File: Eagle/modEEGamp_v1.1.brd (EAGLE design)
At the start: 111.1 x 72.4 mm, 120 parts, among them IC2 INA217P, IC204 TLC277P, IC4 INA217P, P1 20k, P203 20k, Q1 BC547, Q2 BC557, Q202 BC557, Q204 BC557, Q206 BC547, Q208 BC547, Q3 BC547, Q4 BC557

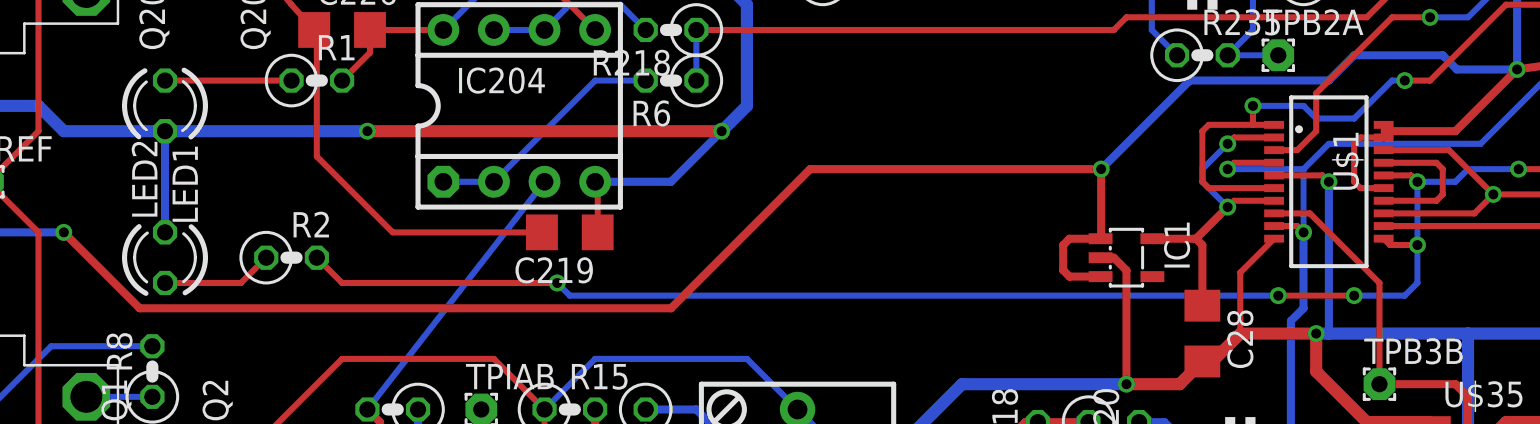
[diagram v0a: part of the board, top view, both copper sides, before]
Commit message: Updated resistor values
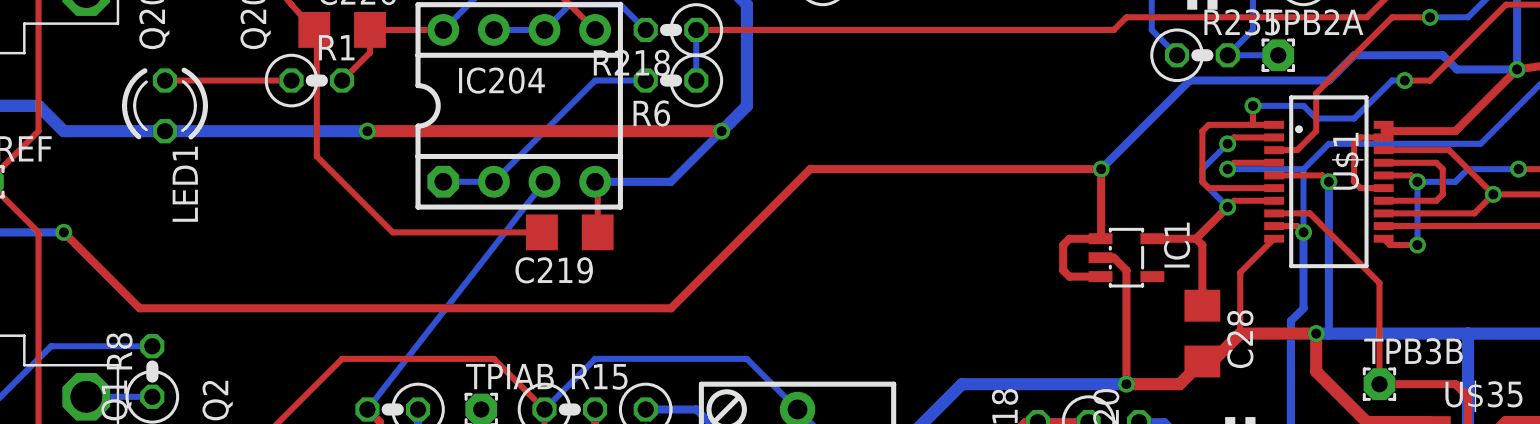
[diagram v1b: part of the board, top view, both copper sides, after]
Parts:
- removed LED2: (no value), led:LED3MM
- removed R2: (no value), resistor:0207/2V
- R1: value (none) -> 1.65k
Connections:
- removed net N$67: LED2.A, R2.1
- net AGND: no longer LED2.K
- net N$8: no longer R2.2
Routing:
- net N$8: track 87.6 -> 29.4 mm, vias 6 -> 3
- net N$67: track 5.61 -> 0.00 mm
- net AGND: track 443.4 -> 438.3 mm
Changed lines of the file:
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@@
 </element>
 <element name="LED1" library="led" package="LED3MM" value="" x="16.51" y="40.64" rot="R270"/>
-<element name="R1" library="resistor" package="0207/2V" value="" x="24.13" y="41.91"/>
-<element name="R2" library="resistor" package="0207/2V" value="" x="22.86" y="33.02"/>
-<element name="LED2" library="led" package="LED3MM" value="" x="16.51" y="33.02" rot="R90"/>
+<element name="R1" library="resistor" package="0207/2V" value="1.65k" x="24.13" y="41.91"/>
 </elements>
 <signals>
@@
 <wire x1="5.715" y1="40.64" x2="5.715" y2="41.91" width="0.4064" layer="1"/>
 <contactref element="LED1" pad="K"/>
-<contactref element="LED2" pad="K"/>
-<wire x1="16.51" y1="39.37" x2="16.51" y2="34.29" width="0.4064" layer="16"/>
 <wire x1="70.485" y1="29.21" x2="70.485" y2="32.277" width="0.3048" layer="1"/>
 <wire x1="70.485" y1="32.277" x2="72.18" y2="33.972" width="0.3048" layer="1"/>
@@
 <wire x1="84.455" y1="37.465" x2="101.4984" y2="37.465" width="0.3048" layer="1"/>
 <wire x1="101.4984" y1="37.465" x2="101.6" y2="37.5666" width="0.3048" layer="1"/>
-<contactref element="R2" pad="2"/>
-<wire x1="79.375" y1="33.655" x2="79.375" y2="31.75" width="0.3048" layer="16"/>
-<wire x1="79.375" y1="31.75" x2="78.74" y2="31.115" width="0.3048" layer="16"/>
-<wire x1="78.74" y1="31.115" x2="76.2" y2="31.115" width="0.3048" layer="16"/>
-<via x="76.2" y="31.115" extent="1-16" drill="0.5"/>
-<wire x1="76.2" y1="31.115" x2="72.39" y2="31.115" width="0.3048" layer="1"/>
-<via x="72.39" y="31.115" extent="1-16" drill="0.5"/>
-<wire x1="72.39" y1="31.115" x2="36.83" y2="31.115" width="0.3048" layer="16"/>
-<wire x1="36.83" y1="31.115" x2="36.195" y2="31.75" width="0.3048" layer="16"/>
-<via x="36.195" y="31.75" extent="1-16" drill="0.5"/>
-<wire x1="36.195" y1="31.75" x2="25.4" y2="31.75" width="0.3048" layer="1"/>
-<wire x1="25.4" y1="31.75" x2="24.13" y2="33.02" width="0.3048" layer="1"/>
 </signal>
 <signal name="N$4">
@@
 <wire x1="22.86" y1="41.91" x2="16.51" y2="41.91" width="0.3048" layer="1"/>
 </signal>
-<signal name="N$67">
-<contactref element="R2" pad="1"/>
-<contactref element="LED2" pad="A"/>
-<wire x1="16.51" y1="31.75" x2="20.32" y2="31.75" width="0.3048" layer="1"/>
-<wire x1="20.32" y1="31.75" x2="21.59" y2="33.02" width="0.3048" layer="1"/>
-</signal>
 </signals>

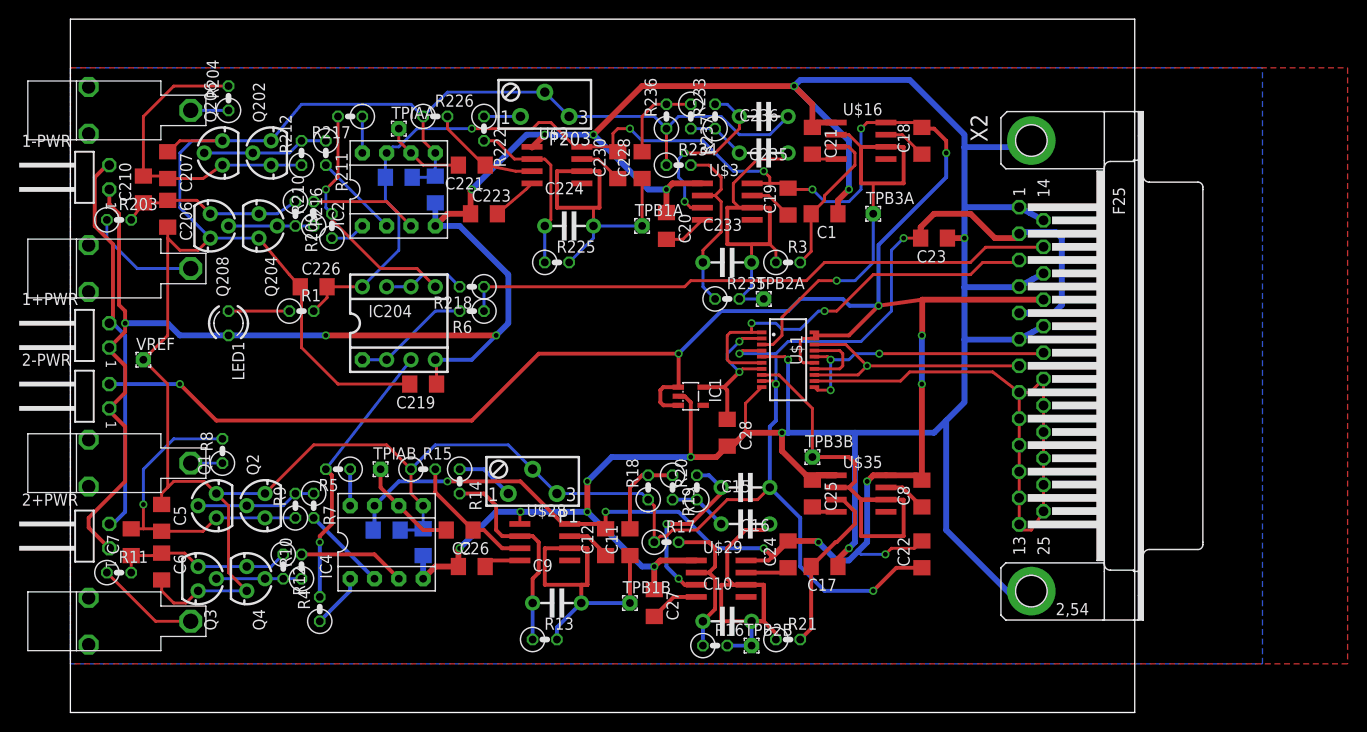
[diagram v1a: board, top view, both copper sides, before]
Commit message: Shrunk boards
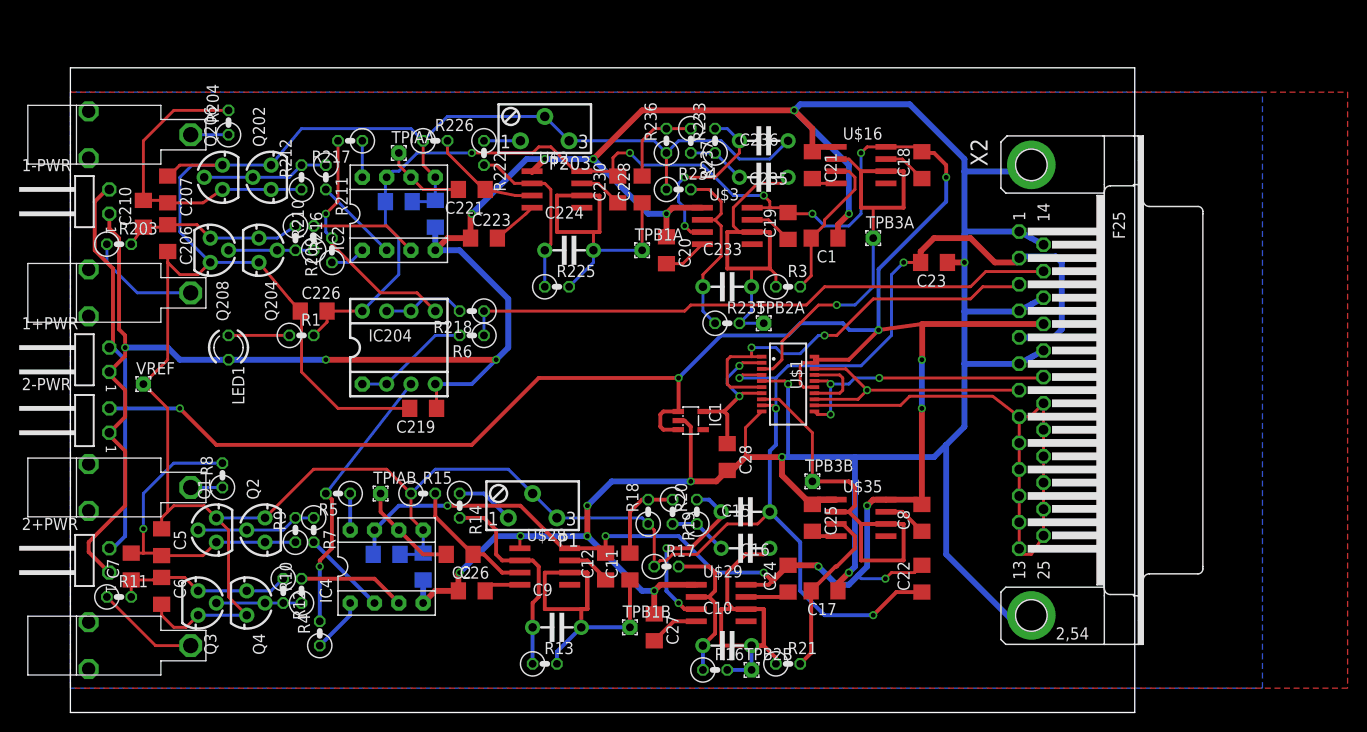
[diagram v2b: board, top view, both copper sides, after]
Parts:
- moved C19 2.54 mm to (74.9, 50.8)
- moved C226 2.54 mm to (25.4, 41.9)
- moved R204 2.54 mm to (16.5, 61.6)
- moved R218 2.54 mm to (41.9, 41.9)
- moved U$3 2.54 mm to (68.6, 50.8)
- moved 2-PWR 2.54 mm to (2.54, 30.5)
- moved C16 2.54 mm to (70.5, 21.0)
- moved IC1 2.54 mm to (64.8, 30.5)
- moved R18 2.54 mm to (60.3, 21.0)
- moved R19 2.54 mm to (62.9, 21.0)
- moved R20 2.54 mm to (65.4, 21.0)
- moved TPB3B 2.54 mm to (77.5, 24.1)
- moved C11 2.54 mm to (58.4, 15.2)
- moved C12 2.54 mm to (55.9, 15.2)
- moved C17 2.54 mm to (78.7, 12.7)
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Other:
- board size 111.1 x 72.4 mm -> 111.1 x 67.3 mm

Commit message: Board shrink
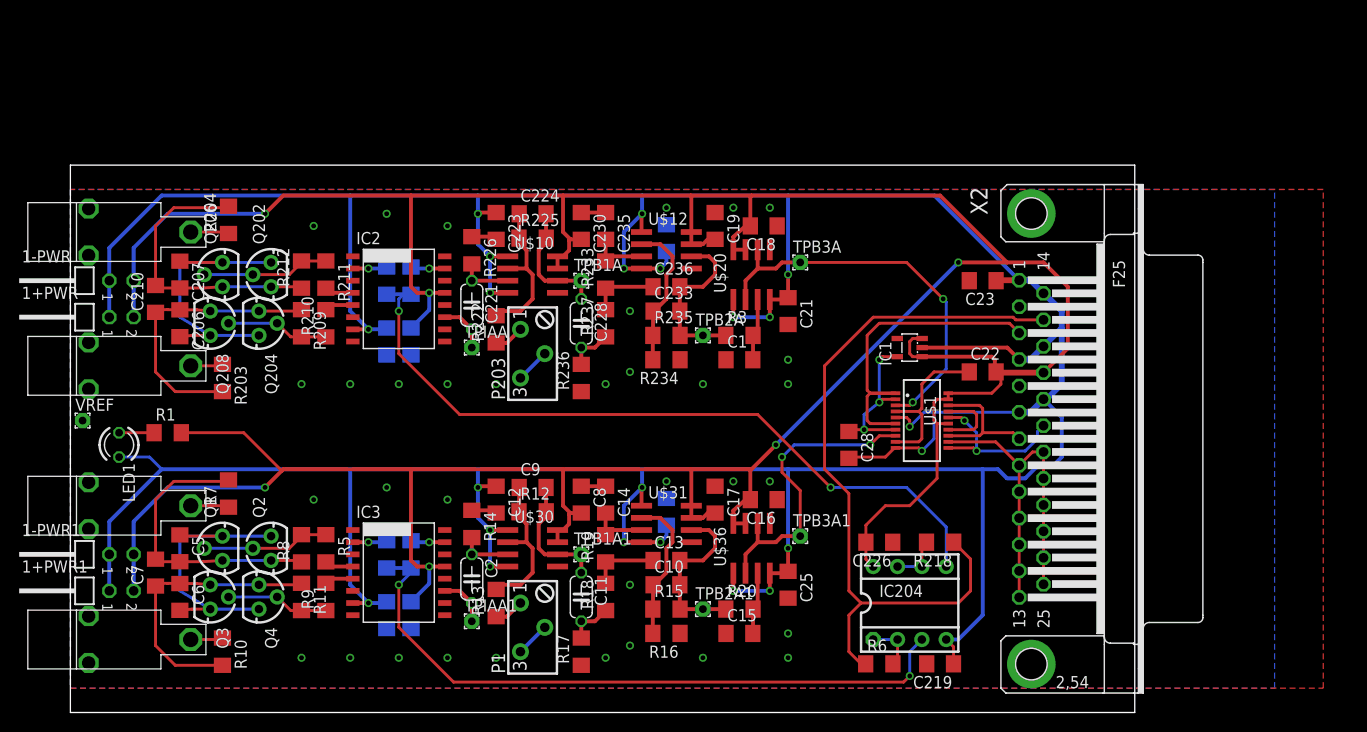
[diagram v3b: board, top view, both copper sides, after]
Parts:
- removed 2+PWR, 2-PWR: TSW-102-02-S-S-RA, con-samtec:TSW-102-02-S-S-RA
- removed C2+, C2-: DIN42802, modEEG:DIN42802
- removed C26, C27: 100nF, resistor:C1206
- removed IC4: INA217P, burr-brown:DIL08
- removed R21: 7.5k, resistor:0207/2V
- removed TPB1B, TPB2B, TPB3B, TPIAB: (no value), WIREPAD:1,6/0,8
- removed U$16, U$2, U$28, U$29, U$3, U$35: AD8021, EEG:SOIC8
- added 1+PWR1, 1-PWR1: TSW-101-02-S-D-RA, con-samtec:TSW-101-02-S-D-RA
- added C1+1, C1-1: DIN42802, modEEG:DIN42802
- added C13: 33nF 5%, resistor:C1206
- added C14: 220nF 5%, resistor:C1206
- added IC3: INA217DW, burr-brown:DW_RPDSO-G16
- added R2: 2k2, resistor:R1206
- added TPB1A1, TPB2A1, TPB3A1, TPIAA1: (no value), WIREPAD:1,6/0,8
- added U$10, U$12, U$20, U$30, U$31, U$36: AD8021, EEG:SOIC8
- 1+PWR, 1-PWR: value TSW-102-02-S-S-RA -> TSW-101-02-S-D-RA; device con-samtec:TSW-102-02-S-S-RA -> con-samtec:TSW-101-02-S-D-RA
- C10, C224, C233, C235, C236, C9: device DISCRETE:C-5 -> resistor:C1206
- C11, C2, C221, C228: device resistor:C1206 -> resistor:C050-024X044
- C15: value 33nF 5% -> 220nf; device DISCRETE:C-5 -> resistor:C1206
- C16: value 220nF 5% -> 100nF; device DISCRETE:C-5 -> resistor:C1206
- C17: value 220nf -> 100nF
- IC2: value INA217P -> INA217DW; device burr-brown:DIL08 -> burr-brown:DW_RPDSO-G16
- R1, R10, R11, R203, R204, R209, R210, R211, R212, R216, R217, R218, R222, R225, R226, R233, R234, R235, R236, R237, R3, R4, R5, R6, R7, R8, R9: device resistor:0207/2V -> resistor:R1206
- R12: value 2k2 -> 100k; device resistor:0207/2V -> resistor:R1206
- R13: value 100k -> 1k; device resistor:0207/2V -> resistor:R1206
- R14: value 1k -> 1M; device resistor:0207/2V -> resistor:R1206
- R15: value 1M -> 100k; device resistor:0207/2V -> resistor:R1206
- R16: value 100k -> 8.2k; device resistor:0207/2V -> resistor:R1206
- R17: value 8.2k -> 1M; device resistor:0207/2V -> resistor:R1206
- R18: value 1M -> 10k; device resistor:0207/2V -> resistor:R1206
- R19: value 10k -> 15k; device resistor:0207/2V -> resistor:R1206
- R20: value 15k -> 7.5k; device resistor:0207/2V -> resistor:R1206
- moved C226 63.8 mm to (84.5, 17.8), turned to 180 degrees
- moved C219 60.2 mm to (90.8, 5.08)
- moved IC204 59.6 mm to (87.6, 11.4)
- moved R6 54.6 mm to (84.5, 5.08), turned to 0 degrees
- moved R218 54.5 mm to (90.8, 17.8)
- moved C8 35.6 mm to (53.3, 22.2), turned to 270 degrees
- moved R15 28.1 mm to (62.2, 10.8)
- moved R12 27.3 mm to (48.3, 21.0), turned to 0 degrees
- moved R236 26.3 mm to (53.3, 34.9)
- moved IC1 24.1 mm to (87.6, 38.1), turned to 90 degrees
- moved P203 23.5 mm to (48.3, 37.5), turned to 90 degrees
- moved C22 22.5 mm to (95.2, 35.6), turned to 0 degrees
- moved TPIAA 21.7 mm to (41.9, 38.1)
- moved R237 21.0 mm to (55.9, 40.6), turned to 90 degrees
- moved R11 19.0 mm to (24.1, 12.1), turned to 270 degrees
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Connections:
- net N$7 renamed SCK
- net N$8 renamed CNV
- removed net N$10: C1.2, R3.2, U$16.3
- removed net N$5 (its old number): C233.2, C236.2, R235.2, R3.1, TPB2A.1, U$3.6
- removed net N$55: C18.1, U$16.7
- removed net N$56: C19.1, U$3.7
- removed net N$58: C20.2, U$3.4
- removed net N$59: C21.2, U$16.4
- removed net N$60: C8.1, U$35.7
- removed net N$61: C12.1, U$28.7
- removed net N$62: C24.1, U$29.7
- removed net N$63: C25.2, U$35.4
- removed net N$64: C26.2, U$28.4
- removed net N$65: C27.2, U$29.4
- net +5V/2: now also 1+PWR1.2, 1-PWR1.2, C16.2, C17.2, IC2.13, IC3.13, U$10.7, U$10.8, U$12.7, U$12.8, U$20.7, U$20.8, U$30.7, U$30.8, U$31.7, U$31.8, U$36.7, U$36.8; no longer 2+PWR.2, 2-PWR.2, C12.2, C24.2, IC2.7, IC4.7, U$16.8, U$2.8, U$28.8, U$29.8, U$3.8, U$35.8
- net ADIN0: now also U$20.2, U$20.6; no longer U$16.2, U$16.6
- net ADIN1: now also TPB3A1.1, U$36.2, U$36.6; no longer TPB3B.1, U$35.2, U$35.6
- net AGND: now also 1+PWR1.1, 1-PWR1.1, C12.1, C24.1, IC2.7, IC3.7, U$10.1, U$10.4, U$12.1, U$12.4, U$20.1, U$20.4, U$30.1, U$30.4, U$31.1, U$31.4, U$36.1, U$36.4; no longer 2+PWR.1, 2-PWR.1, C1.1, C17.1, C26.1, C27.1, IC2.4, IC4.4, U$16.1, U$2.1, U$28.1, U$29.1, U$3.1, U$35.1
- net N$13: now also C233.2, C236.2, R235.2, R3.1, TPB2A.1, U$12.6; no longer IC204.3, R4.2, R5.2
- net N$14: now also IC2.2; no longer IC2.1
- net N$15: now also C1.2, R3.2, U$20.3; no longer C2.2, IC4.6, TPIAB.1
- net N$16: now also IC204.3, R2.2, R4.2; no longer IC4.2, R7.2
- net N$17: now also C2.2, IC3.11, TPIAA1.1; no longer IC4.3, R10.2
- net N$18: now also IC3.4, R5.2; no longer Q1.2, Q2.2, R7.1, R9.2
- net N$19: now also IC3.5, R9.2; no longer C5.2, C7.2, Q1.3, Q2.3, R8.2, R9.1
- net N$20: now also IC2.15; no longer IC2.8
- net N$21: now also IC2.4; no longer IC2.2
- net N$22: now also Q1.2, Q2.2, R5.1, R8.2; no longer Q3.2, Q4.2, R10.1, R12.2
- net N$23: now also C5.2, C7.2, Q1.3, Q2.3, R7.2, R8.1; no longer C6.1, C7.1, Q3.3, Q4.3, R11.2, R12.1
- net N$24: now also Q3.2, Q4.2, R11.2, R9.1; no longer C2-.P$1, R8.1
- net N$25: now also IC2.11; no longer IC2.6
- net N$26: now also C6.1, C7.1, Q3.3, Q4.3, R10.2; no longer C2+.P$1
- net N$27: now also IC2.5; no longer IC2.3
- net N$28: now also U$10.3; no longer U$2.3
- net N$30: now also C1-1.P$1, R7.1; no longer C2.1, R15.2, U$28.3
- net N$31: now also C1+1.P$1, R10.1; no longer C9.1, R13.1, R14.2, U$28.2
- net N$33: now also C2.1, R14.2, U$30.3; no longer P1.1, R14.1
- net N$34: now also C9.1, R12.1, U$30.2; no longer C11.1, C9.2, TPB1B.1, U$28.6
- net N$36: now also P1.1, R13.1; no longer C15.1, R19.2, R20.1
- net N$37: now also C11.1, C9.2, R12.2, TPB1A1.1, U$30.6; no longer C16.2, R20.2, U$29.3
- net N$38: now also U$10.2; no longer U$2.2
- net N$41: now also C13.1; no longer C11.2
- net N$42: now also U$10.6; no longer U$2.6
- net N$44: now also C14.2, R19.2, U$31.3; no longer C10.1, R16.1, R17.2, U$29.2
- net N$45: now also C11.2, R17.2, R18.1; no longer IC4.1, R4.1
- net N$46: now also C10.1, R15.1, R16.2, U$31.2; no longer IC4.8, R5.1
- net N$47: now also IC3.2, R2.1; no longer C10.2, C15.2, R16.2, R21.1, TPB2B.1, U$29.6
- net N$48: now also IC3.15, R4.1; no longer C17.2, R21.2, U$35.3
- net N$49: now also U$12.2; no longer U$3.2
- net N$53: now also C10.2, C13.2, R15.2, R20.1, TPB2A1.1, U$31.6; no longer C230.1, U$2.7
- net N$54: now also C15.2, R20.2, U$36.3; no longer C223.2, U$2.4
- net N$57: now also U$12.3; no longer U$3.3
- net VCOM: now also C1.1, C12.2, C14.1, C15.1, C17.1, C18.1, C19.1, C20.2, C21.2, C223.2, C230.1, C24.2, C25.2, C8.1, IC2.10, IC3.10, R14.1, R16.1; no longer IC2.5, IC4.5, R15.1, R18.1
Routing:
- net VCOM: track 377.1 -> 97.9 mm, vias 4 -> 34
- net N$16: track 8.98 -> 69.6 mm, vias 0 -> 2
- net N$12: track 25.3 -> 78.5 mm, vias 1 -> 2
- net N$19: track 33.6 -> 3.24 mm, vias 1 -> 0
- net N$5 (its old number): track 29.7 -> 0.00 mm
- net AGND: track 438.3 -> 460.2 mm, vias 19 -> 22
- net N$47: track 25.3 -> 3.59 mm, vias 0 -> 1
- net N$31: track 22.3 -> 3.38 mm
- net N$26: track 10.9 -> 29.5 mm
- net N$3: track 57.4 -> 39.2 mm
- net N$10: track 16.0 -> 0.00 mm
- net N$48: track 18.3 -> 3.59 mm, vias 0 -> 1
- net N$66: track 62.7 -> 77.1 mm
- net SCK: track 28.2 -> 14.5 mm, vias 1 -> 0
- net N$53: track 4.59 -> 18.1 mm
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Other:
- board size 111.1 x 67.3 mm -> 111.1 x 57.1 mm

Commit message: Changed to DB-15 connector
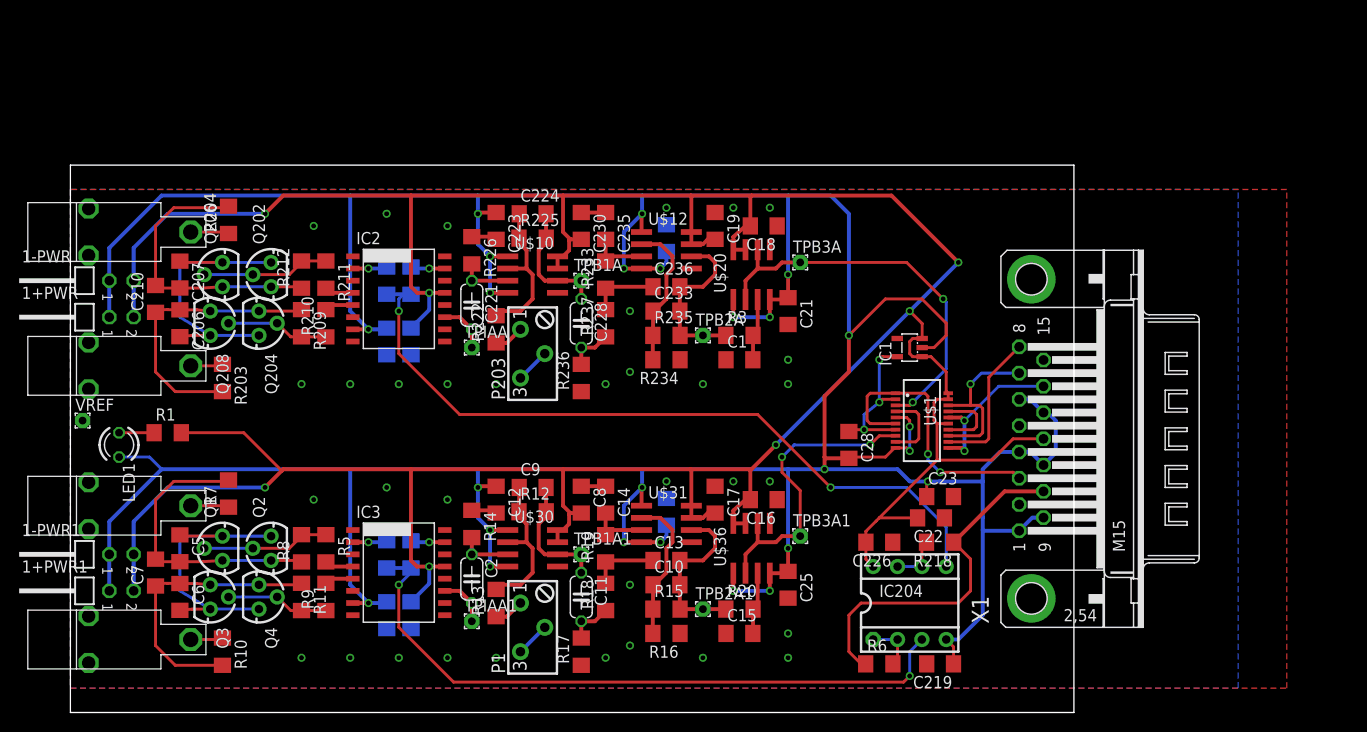
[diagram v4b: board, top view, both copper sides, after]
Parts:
- removed X2: (no value), con-subd:F25HP
- added X1: (no value), con-subd:M15HP
- moved C23 23.0 mm to (90.8, 22.5), turned to 0 degrees
- moved C22 16.2 mm to (89.9, 20.3), turned to 180 degrees
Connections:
- net +5V/2: now also X1.12; no longer X2.17
- net AGND: now also X1.1, X1.11, X1.13, X1.4, X1.6, X1.9; no longer X2.1, X2.14, X2.16, X2.18, X2.4, X2.6
- net CNV: now also X1.14; no longer X2.19
- net N$1: now also X1.3; no longer X2.3
- net N$3: now also X1.8; no longer X2.10, X2.11, X2.12, X2.13, X2.20, X2.21, X2.22, X2.23, X2.24, X2.25, X2.8, X2.9
- net N$66: now also X1.10; no longer X2.15
- net SCK: now also X1.7; no longer X2.7
- net VCOM: now also X1.2, X1.5; no longer X2.2, X2.5
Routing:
- net N$66: track 77.1 -> 37.2 mm
- net +5V/2: track 380.8 -> 355.5 mm, vias 6 -> 7
- net N$3: track 39.2 -> 15.3 mm
- net AGND: track 460.2 -> 444.0 mm, vias 22 -> 25
- net VCOM: track 97.9 -> 88.8 mm
- net N$1: track 34.4 -> 29.2 mm, vias 0 -> 2
- net SCK: track 14.5 -> 17.8 mm, vias 0 -> 1
- net CNV: track 17.1 -> 16.6 mm
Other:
- board size 111.1 x 57.1 mm -> 104.8 x 57.1 mm
